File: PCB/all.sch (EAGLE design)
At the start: 127 parts, among them J1 micro USB, J2 LIPO-BATTERY-CONNECTOR, J3 Qi coil, J4 Qi coil, J5 Qi coil, J6 Qi coil, J8 BL-HP20AUW2C, Q1 NPN, Q2 NPN, Q3 8MHz, U1 ATMEGA32U4QFN, U2 LM3671, U3 MPU-6050-1, U4 BQ51013B_RHL_20, U5 MCP73831, U6 CAT4139, U7 BQ51013B_RHL_20, U8 BQ51013B_RHL_20, U9 BQ51013B_RHL_20

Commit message: routing finished
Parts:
- added C4: 0.1μF, rcl:C-EUC0603K
- CP1, CP3, CP5, CP7: value 18pF -> 2.2nF
- CP2, CP4, CP6, CP8, CS, CS10, CS27, CS30: value 18pF -> x
- CS17, CS20, CS37, CS7: value 18pF -> 220nF
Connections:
- net 3.3V: now also C4.1
- net GND: now also C4.2
- net PWM: now also U1.PB7
- net RGB: now also U1.PE6
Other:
- moved on the sheet: C10, C11, C12

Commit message: version 3.0 complete release
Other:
- note added: "Make sure all capacitors on the RECT pin are rated at more than 7V!"
- note added: "Tako care if regulator end with -ADJ and add resistor and capacitors in the feedback!"
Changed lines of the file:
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@@
 <?xml version="1.0" encoding="utf-8"?>
 <!DOCTYPE eagle SYSTEM "eagle.dtd">
-<eagle version="7.6.0">
+<eagle version="7.7.0">
 <drawing>
 <settings>
@@
 <text x="208.28" y="134.62" size="1.27" layer="97">I_LED = 0.3V / R19</text>
 <text x="240.284" y="144.272" size="1.27" layer="97">White LED</text>
+<text x="101.6" y="137.16" size="1.778" layer="97">Tako care if regulator end with -ADJ and add
+resistor and capacitors in the feedback!</text>
 </plain>
 <instances>
@@
 Pero 2016</text>
 <text x="345.44" y="20.32" size="2.54" layer="97">Qi chargers</text>
+<text x="88.9" y="218.44" size="2.54" layer="97">Make sure all capacitors on the RECT pin
+are rated at more than 7V!</text>
 </plain>
 <instances>

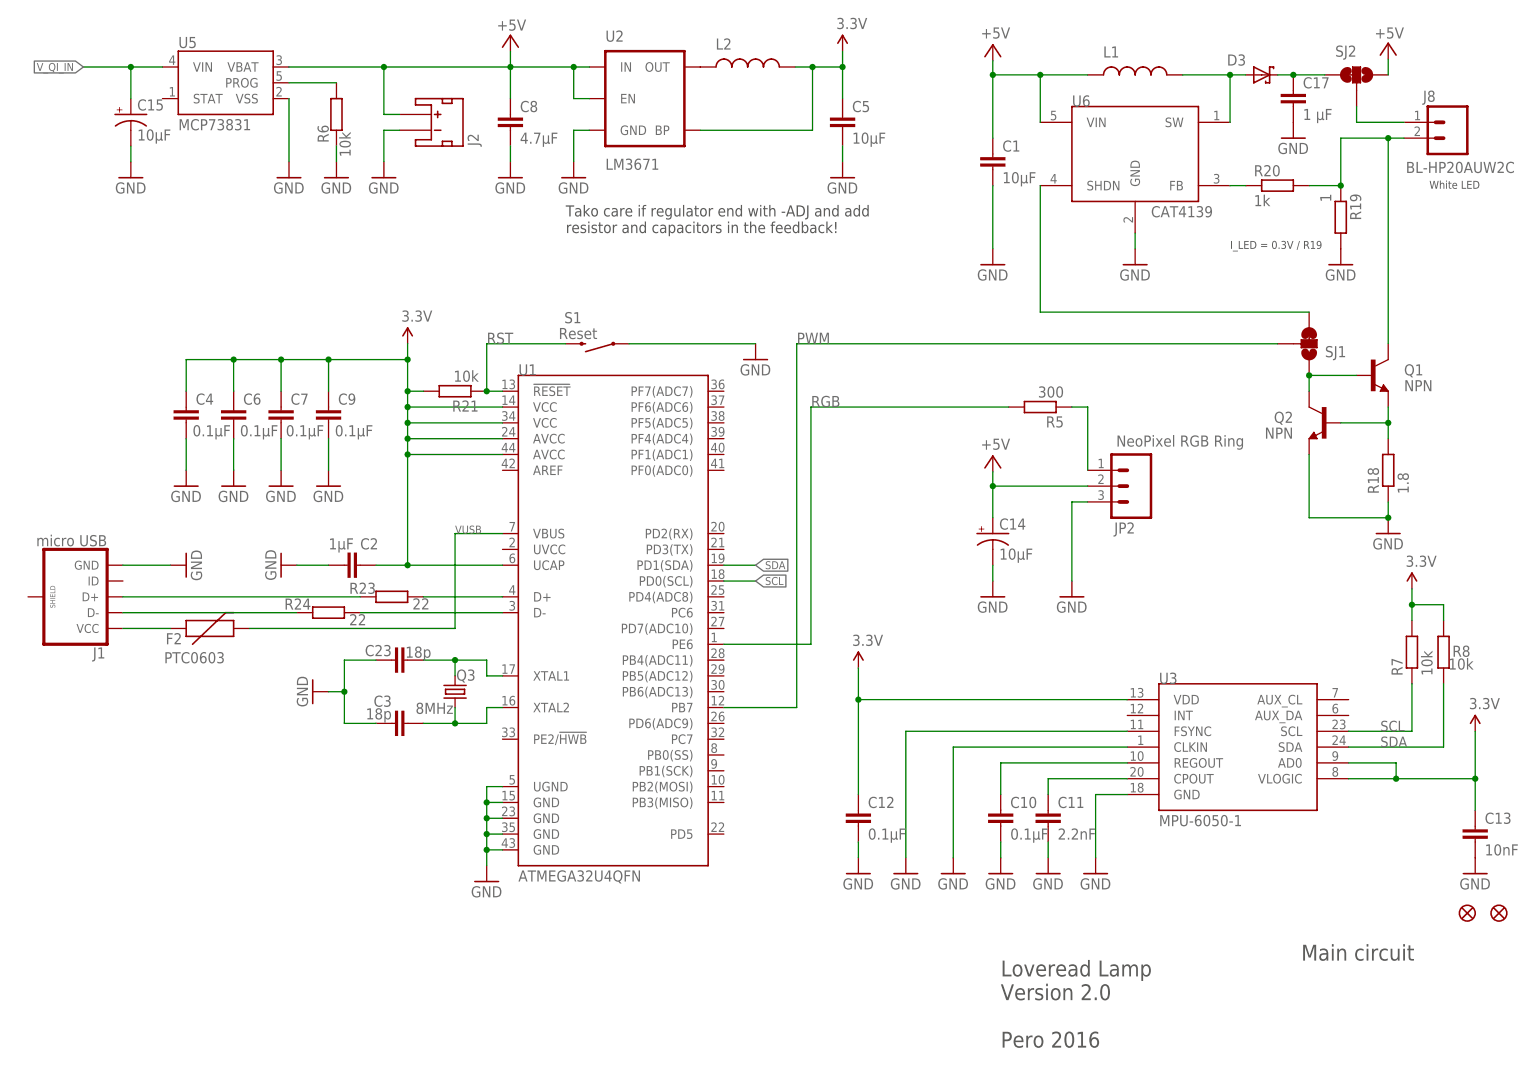
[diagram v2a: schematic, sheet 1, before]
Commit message: no xtal and no transistor LED drivers
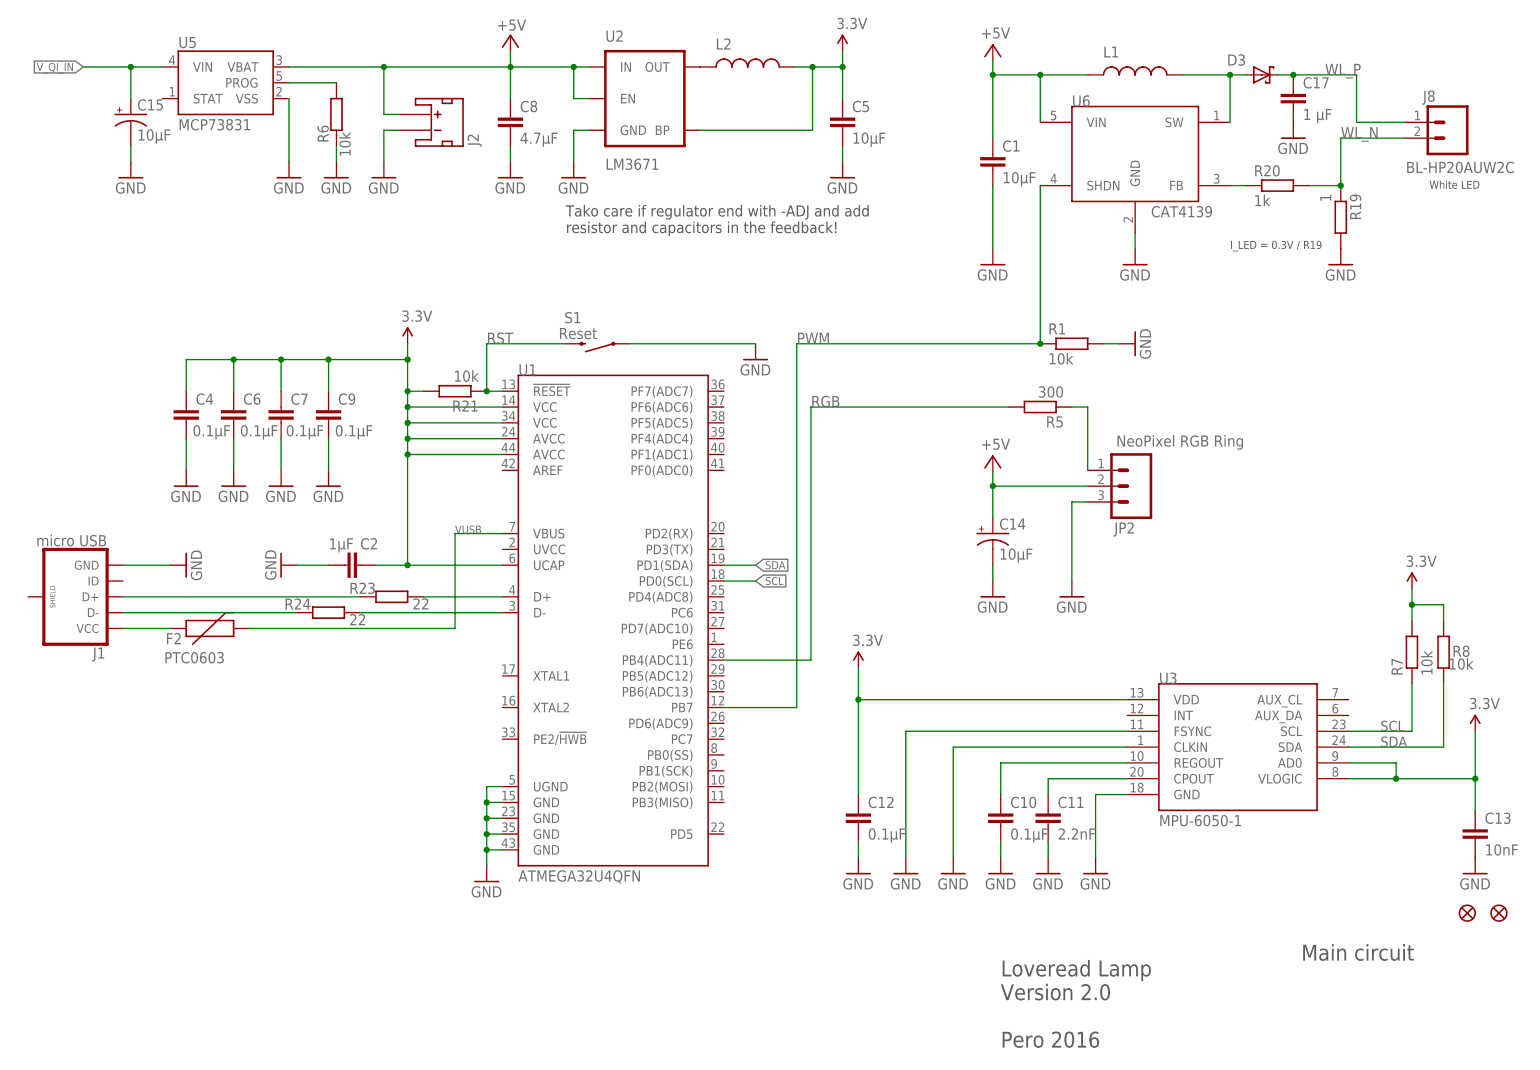
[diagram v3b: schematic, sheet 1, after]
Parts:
- removed C23, C3: 18p, rcl:C-EUC0603
- removed Q1, Q2: NPN, SparkFun-DiscreteSemi:TRANSISTOR_NPNSOT23-3
- removed Q3: 8MHz, pero_library:QUARTZ-CRYSTAL-8MHZQC6CB8.00000F18B23R
- removed R18: 1.8, rcl:R-EU_R0603
- removed SJ1, SJ2: JUMPER-PAD-3-2OF3_NC_BY_TRACE_SMALL, SparkFun-Passives:JUMPER-PAD-3-2OF3_NC_BY_TRACE_SMALL
- added R1: 10k, resistor:R-EU_R0603
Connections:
- removed net N$18: J8.2, Q1.C, R19.1, R20.2
- removed net N$2: Q1.E, Q2.B, R18.2
- removed net N$3: Q1.B, Q2.C, SJ1.1
- removed net N$4: SJ1.3, U6.SHDN
- removed net N$62: J8.1, SJ2.2
- removed net N$64: C17.1, D3.C, SJ2.3
- removed net N$71: C23.2, Q3.2, U1.XTAL1
- removed net N$72: C3.2, Q3.1, U1.XTAL2
- new net WL_N: J8.2, R19.1, R20.2
- new net WL_P: C17.1, D3.C, J8.1
- net +5V: no longer SJ2.1
- net GND: now also R1.2; no longer C23.1, C3.1, Q2.E, R18.1
- net PWM: now also R1.1, U6.SHDN; no longer SJ1.2
- net RGB: now also U1.PB4(ADC11); no longer U1.PE6

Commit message: qi coil switch prototype
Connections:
- net WL_N renamed WL_CA
- net WL_P renamed WL_AN
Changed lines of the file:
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@@
 </segment>
 </net>
-<net name="WL_N" class="0">
+<net name="WL_CA" class="0">
 <segment>
 <pinref part="R19" gate="G$1" pin="1"/>
@@
 </segment>
 </net>
-<net name="WL_P" class="0">
+<net name="WL_AN" class="0">
 <segment>
 <pinref part="D3" gate="G$1" pin="C"/>
